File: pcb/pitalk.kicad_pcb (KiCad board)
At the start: 2 copper layers, 65 x 55 mm, 13 parts, among them J1 RPi_GPIO_40pin_IDC, J2 Screen_Waveshare_2in_Molex_KK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, J3 Mic_INMP441_Male_Header, J4 Speaker_4R_3W, J5 Button_LED_Male_Header, U1 MAX98357A

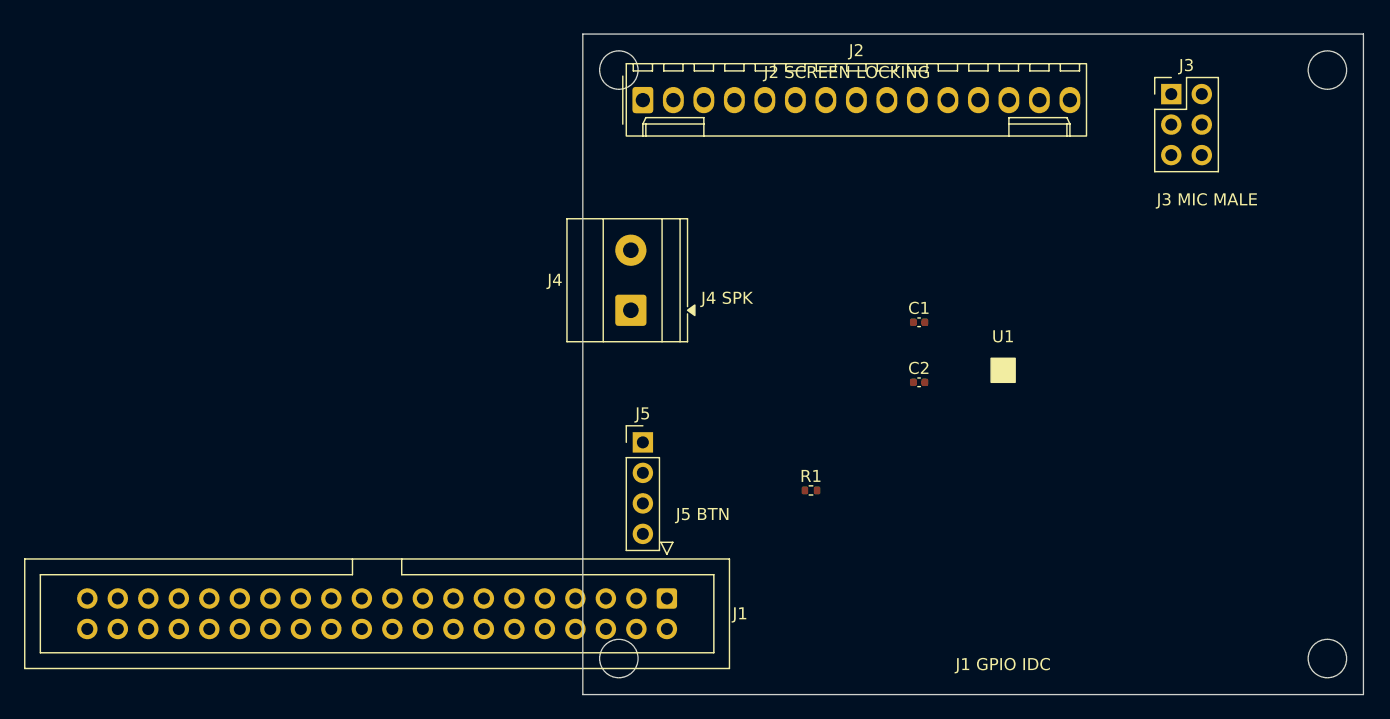
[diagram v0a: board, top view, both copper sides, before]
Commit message: Fix KiCad PCB render framing
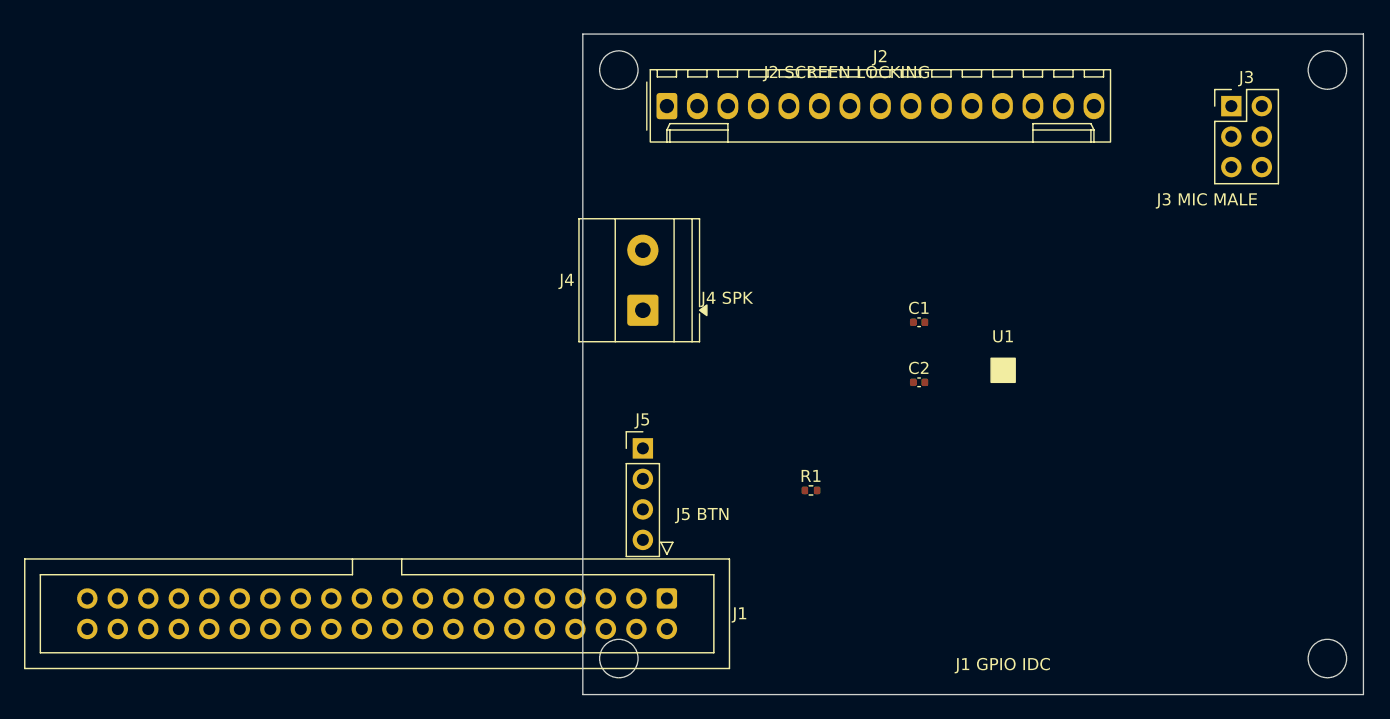
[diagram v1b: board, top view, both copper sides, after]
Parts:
- moved J3 5.10 mm to (54.0, 6.00)
- moved J2 2.06 mm to (7.00, 6.00)
- moved J4 1.00 mm to (5.00, 23.0)
- moved J5 0.50 mm to (5.00, 34.5)
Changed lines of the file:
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@@
 	(generator "kicad-footprint-generator")
 	(layer "F.Cu")
-	(at 5.0 5.5 0)
+	(at 7.0 6.0 0)
 	(descr "Molex KK-254 Interconnect System, old/engineering part number: AE-6410-15A example for new part number: 22-27-2151, 15 Pins (http://www.molex.com/pdm_docs/sd/022272021_sd.pdf)")
 	(tags "connector Molex KK-254 vertical")
@@
 	(generator "kicad-footprint-generator")
 	(layer "F.Cu")
-	(at 49.0 5.0 0)
+	(at 54.0 6.0 0)
 	(descr "Through hole straight pin header, 2x03, 2.54mm pitch, double rows")
 	(tags "Through hole pin header THT 2x03 2.54mm double row")
@@
 	(generator "kicad-footprint-generator")
 	(layer "F.Cu")
-	(at 4.0 23.0 90)
+	(at 5.0 23.0 90)
 	(descr "Terminal Block Phoenix MKDS-1,5-2, 2 pins, pitch 5mm, size 10x9.8mm, drill diameter 1.3mm, pad diameter 2.6mm, http://www.farnell.com/datasheets/100425.pdf")
 	(tags "THT Terminal Block Phoenix MKDS-1,5-2 pitch 5mm size 10x9.8mm drill 1.3mm pad 2.6mm")
@@
 	(generator "kicad-footprint-generator")
 	(layer "F.Cu")
-	(at 5.0 34.0 0)
+	(at 5.0 34.5 0)
 	(descr "Through hole straight pin header, 1x04, 2.54mm pitch, single row")
 	(tags "Through hole pin header THT 1x04 2.54mm single row")

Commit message: Move amplifier to external header
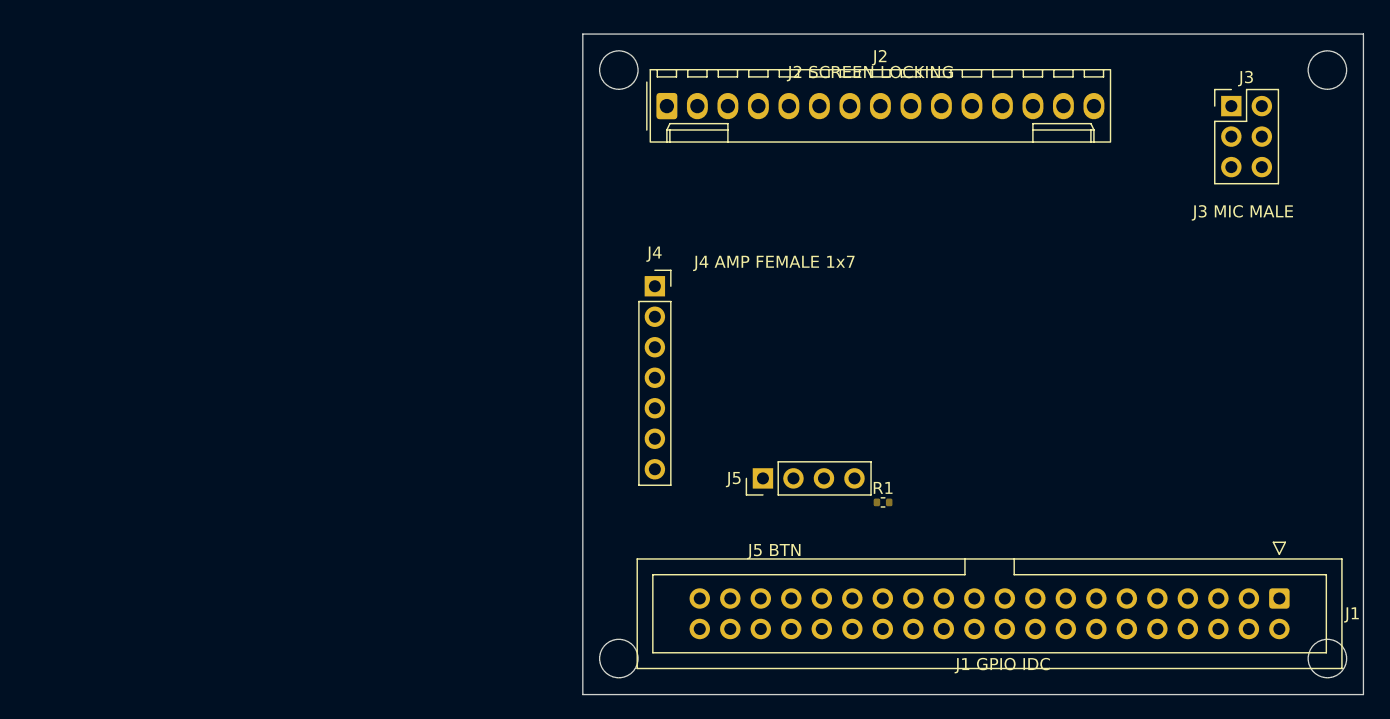
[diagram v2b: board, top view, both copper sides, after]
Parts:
- removed C1: 100nF, Capacitor_SMD:C_0402_1005Metric
- removed C2: 10uF, Capacitor_SMD:C_0402_1005Metric
- removed U1: MAX98357A, Pitalk:MAX98357A_WLCSP9_placeholder
- J4: value Speaker_4R_3W -> External_MAX98357A_Amp_Female; footprint TerminalBlock_Phoenix:TerminalBlock_Phoenix_MKDS-1,5-2_1x02_P5.00mm_Horizontal -> Connector_PinSocket_2.54mm:PinSocket_1x07_P2.54mm_Vertical
- moved J1 51.0 mm to (58.0, 47.0)
- moved J5 10.3 mm to (15.0, 37.0), turned to 90 degrees
- moved R1 6.08 mm to (25.0, 39.0)
- moved J4 2.24 mm to (6.00, 21.0), turned to 0 degrees
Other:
- board text added: "J4 AMP FEMALE 1x7"
- board text removed: "J4 SPK"

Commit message: updates
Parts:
- removed H1, H2, H3, H4: MountingHole, MountingHole:MountingHole_3.2mm_M3
- added C1: 100nF, Capacitor_SMD:C_0402_1005Metric, F.Cu at (40.0, 39.0)
- added C2: 100nF, Capacitor_SMD:C_0402_1005Metric, F.Cu at (45.0, 39.0)
- added MH1: , MountingHole:MountingHole_3.2mm_M3, F.Cu at (3.20, 3.20)
- added MH2: , MountingHole:MountingHole_3.2mm_M3, F.Cu at (61.8, 3.20)
- added MH3: , MountingHole:MountingHole_3.2mm_M3, F.Cu at (3.20, 51.8)
- added MH4: , MountingHole:MountingHole_3.2mm_M3, F.Cu at (61.8, 51.8)
- J5: value Button_LED_Male_Header -> Button_LED
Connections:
- J1 pad 1: (no net) -> +3V3
- J1 pad 12: (no net) -> I2S_BCLK
- J1 pad 13: (no net) -> DISP_RST
- J1 pad 14: (no net) -> GND
- J1 pad 15: (no net) -> BTN_SW
- J1 pad 17: (no net) -> +3V3
- J1 pad 19: (no net) -> SPI_MOSI
- J1 pad 2: (no net) -> +5V
- J1 pad 20: (no net) -> GND
- J1 pad 22: (no net) -> DISP_DC
- J1 pad 23: (no net) -> SPI_SCLK
- J1 pad 24: (no net) -> SPI_CE0
- J1 pad 25: (no net) -> GND
- J1 pad 3: (no net) -> I2C_SDA
- J1 pad 30: (no net) -> GND
- J1 pad 32: (no net) -> DISP_BL
- J1 pad 33: (no net) -> GPIO13
- J1 pad 34: (no net) -> GND
- J1 pad 35: (no net) -> I2S_LRCLK
- J1 pad 38: (no net) -> I2S_DIN
- J1 pad 39: (no net) -> GND
- J1 pad 4: (no net) -> +5V
- J1 pad 40: (no net) -> I2S_DOUT
- J1 pad 5: (no net) -> I2C_SCL
- J1 pad 6: (no net) -> GND
- J1 pad 7: (no net) -> TOUCH_INT
- J1 pad 9: (no net) -> GND
- J2 pad 1: (no net) -> GND
- J2 pad 10: (no net) -> I2C_SDA
- J2 pad 11: (no net) -> I2C_SCL
- J2 pad 12: (no net) -> TOUCH_INT
- J2 pad 13: (no net) -> DISP_BL
- J2 pad 14: (no net) -> GND
- J2 pad 15: (no net) -> +3V3
- J2 pad 2: (no net) -> +3V3
- J2 pad 3: (no net) -> GND
- J2 pad 4: (no net) -> +3V3
- J2 pad 5: (no net) -> SPI_MOSI
- J2 pad 6: (no net) -> SPI_SCLK
- J2 pad 7: (no net) -> SPI_CE0
- J2 pad 8: (no net) -> DISP_DC
- J2 pad 9: (no net) -> DISP_RST
- J3 pad 1: (no net) -> +3V3
- J3 pad 2: (no net) -> I2S_BCLK
- J3 pad 3: (no net) -> GND
- J3 pad 4: (no net) -> I2S_LRCLK
- J3 pad 5: (no net) -> GND
- J3 pad 6: (no net) -> I2S_DIN
- J4 pad 1: (no net) -> +5V
- J4 pad 2: (no net) -> GND
- J4 pad 3: (no net) -> +3V3
- J4 pad 4: (no net) -> GND
- J4 pad 5: (no net) -> I2S_DOUT
- J4 pad 6: (no net) -> I2S_BCLK
- J4 pad 7: (no net) -> I2S_LRCLK
- J5 pad 1: (no net) -> BTN_SW
- J5 pad 2: (no net) -> GND
- J5 pad 3: (no net) -> BTN_LED
- J5 pad 4: (no net) -> GND
- R1 pad 1: (no net) -> GPIO13
- R1 pad 2: (no net) -> BTN_LED
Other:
- board text added: "C1 100nF +3V3"
- board text added: "C2 100nF +5V"
- board text added: "J1 GPIO IDC (to RPi)"
- board text added: "J2 SCREEN (locking)"
- board text added: "J3 MIC (male hdr)"
- board text added: "J4 AMP (female sckt)"
- board text added: "R1 330R BTN_LED"
- board text removed: "J1 GPIO IDC"
- board text removed: "J2 SCREEN LOCKING"
- board text removed: "J3 MIC MALE"
- board text removed: "J4 AMP FEMALE 1x7"
